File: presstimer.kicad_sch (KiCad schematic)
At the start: 28 parts, among them J1 Screw_Terminal_01x02, SW1 SW_Push, SW2 SW_Push, U1 AP7361C-33ER, U2 ESP32-S3-WROOM-1

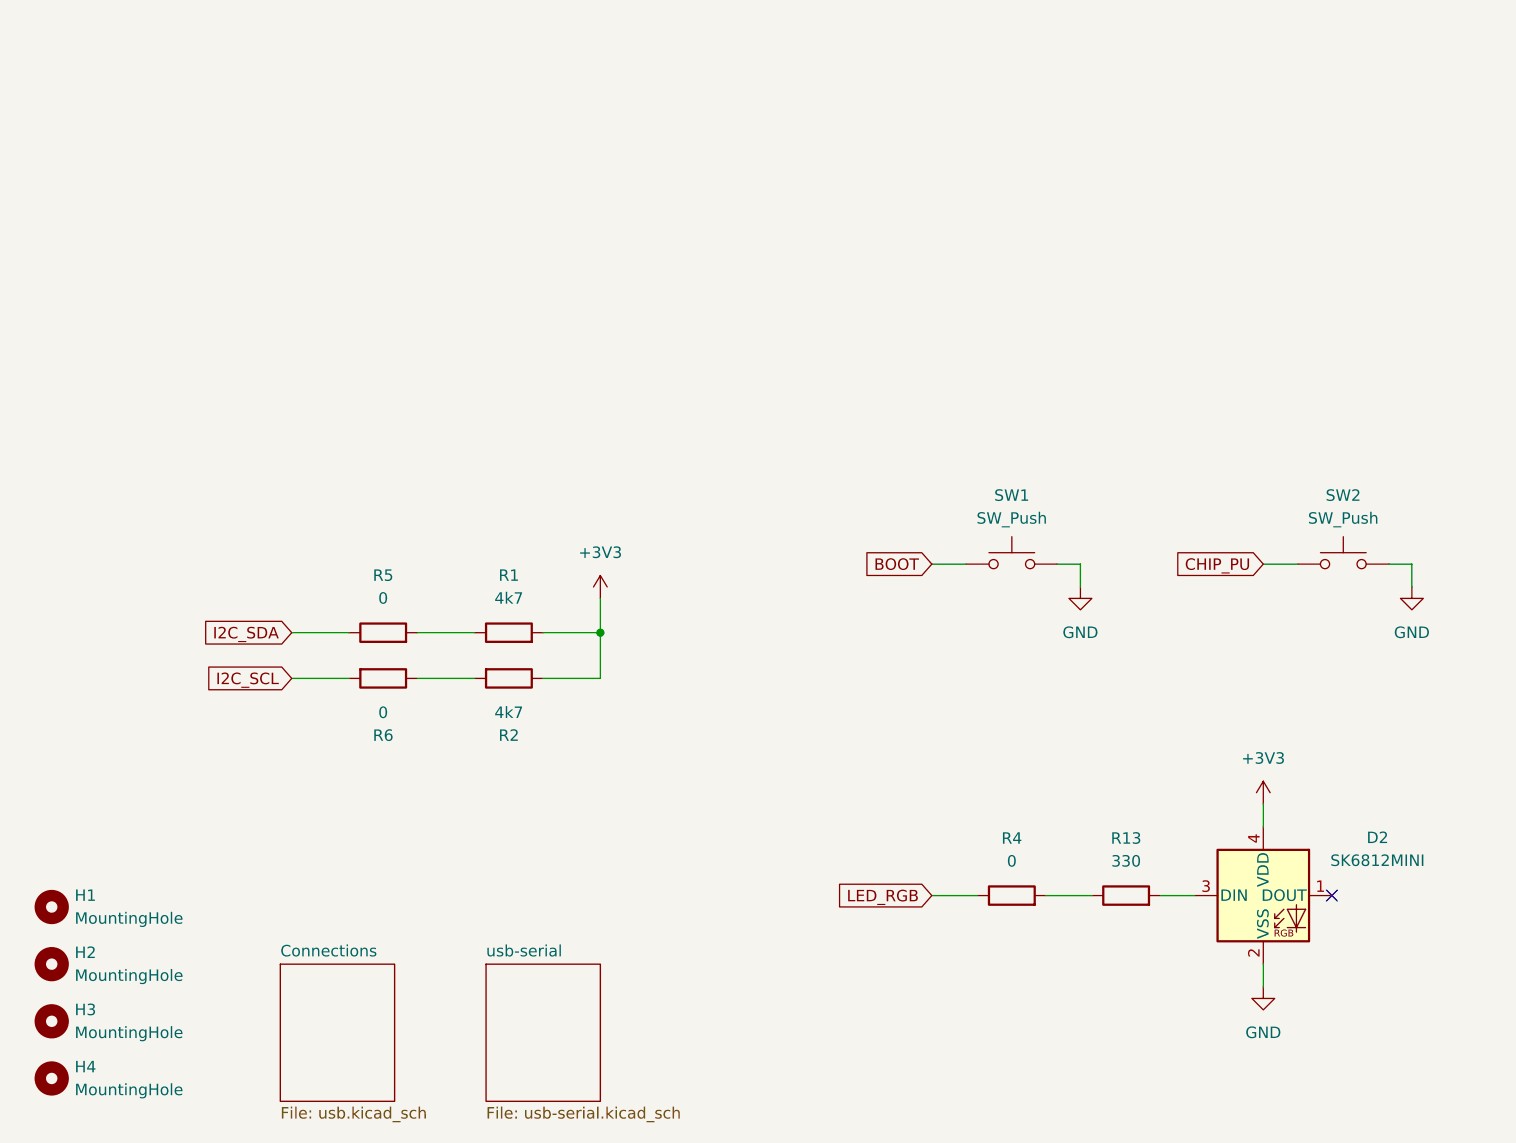
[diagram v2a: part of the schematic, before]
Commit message: before removal of cp2102
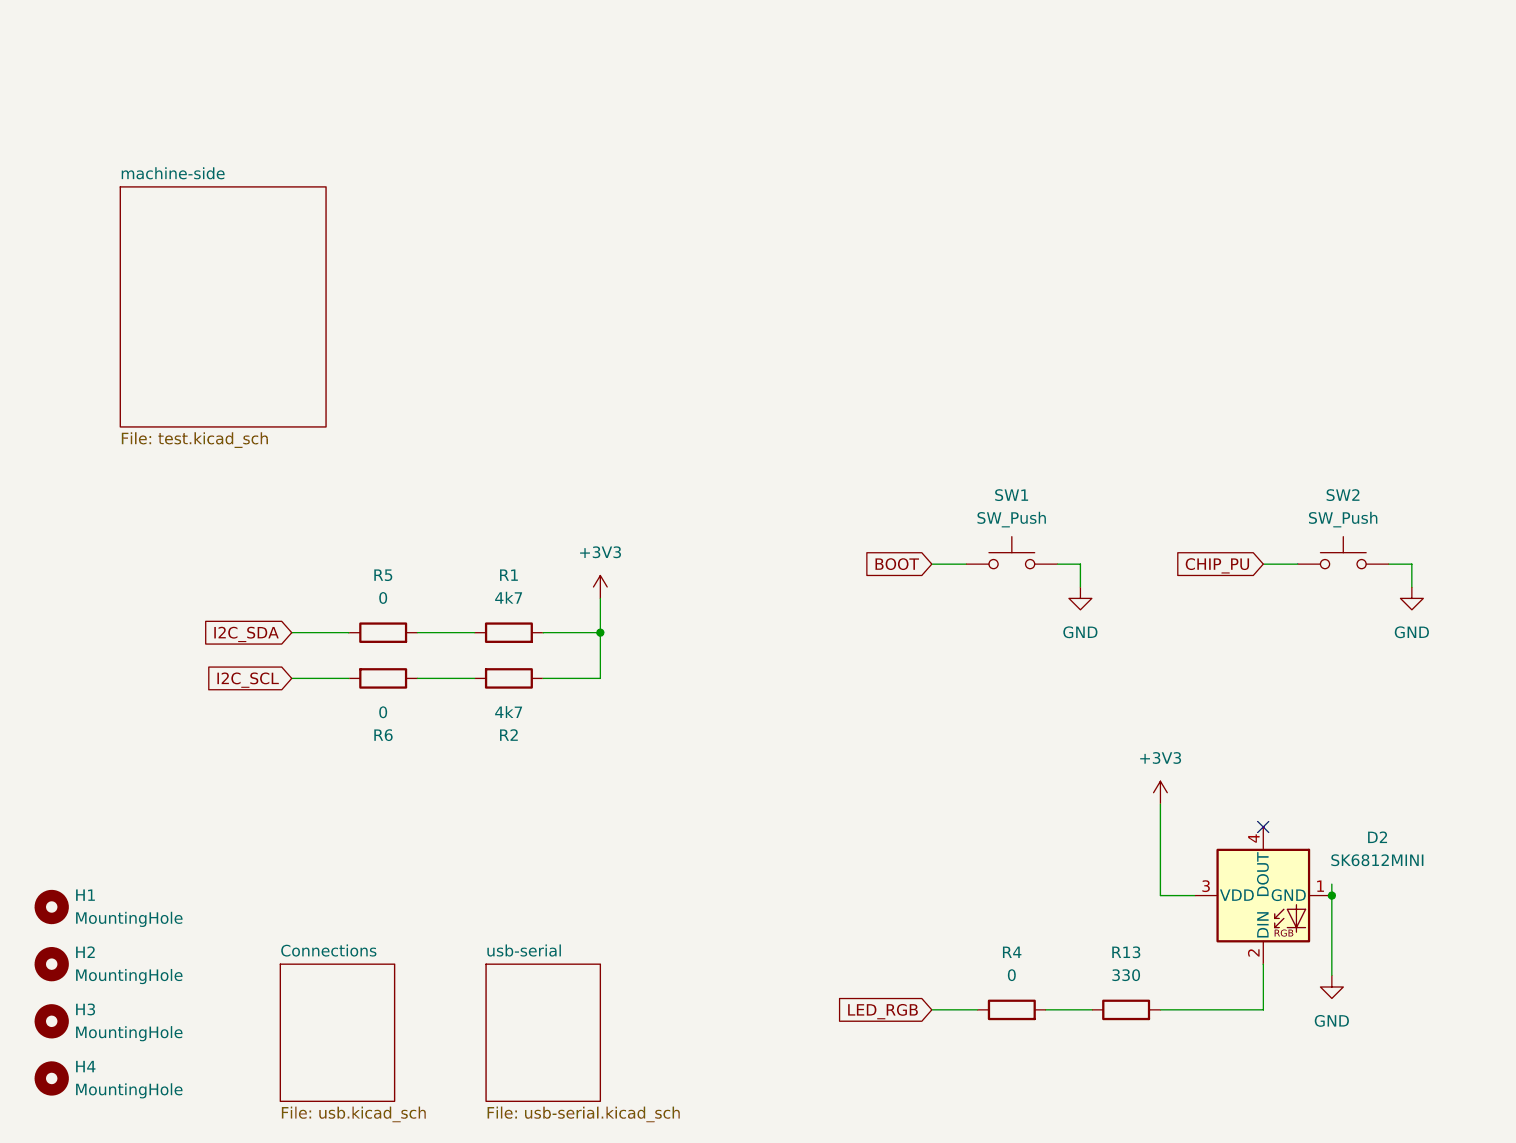
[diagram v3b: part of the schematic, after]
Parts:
- D2: footprint LED_SMD:LED_SK6812MINI_PLCC4_3.5x3.5mm_P1.75mm -> markus:SK6812MINI--HS-012_3.7x3.5mm; symbol LED:SK6812MINI -> markus:SK6812MINI
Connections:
- net +3V3: now also D2.3 (VDD); no longer D2.4 (VDD)
- net GND: now also D2.1 (GND); no longer D2.2 (VSS)
- net at R13.2: now also D2.2 (DIN); no longer D2.3 (DIN)
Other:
- added sheet machine-side (test.kicad_sch)
- moved on the sheet: R13, R4
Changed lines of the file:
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@@
 	)
 	(junction
+		(at 160.02 170.18)
+		(diameter 0)
+		(color 0 0 0 0)
+	)
+	(junction
 		(at 182.88 59.69)
 		(diameter 0)
@@
 	)
 	(no_connect
-		(at 160.02 170.18)
+		(at 152.4 162.56)
 	)
 	(no_connect
@@
 	(wire
 		(pts
+			(xy 160.02 170.18) (xy 160.02 179.07)
+		)
+		(stroke
+			(width 0)
+			(type default)
+		)
+	)
+	(wire
+		(pts
 			(xy 54.61 26.67) (xy 58.42 26.67)
 		)
@@
 	(wire
 		(pts
-			(xy 128.27 170.18) (xy 133.35 170.18)
+			(xy 128.27 182.88) (xy 133.35 182.88)
 		)
 		(stroke
@@
 	(wire
 		(pts
-			(xy 152.4 177.8) (xy 152.4 180.34)
+			(xy 160.02 168.91) (xy 160.02 170.18)
 		)
 		(stroke
@@
 	(wire
 		(pts
+			(xy 140.97 170.18) (xy 144.78 170.18)
+		)
+		(stroke
+			(width 0)
+			(type default)
+		)
+	)
+	(wire
+		(pts
 			(xy 182.88 60.96) (xy 182.88 59.69)
 		)
@@
 	(wire
 		(pts
-			(xy 115.57 170.18) (xy 120.65 170.18)
+			(xy 115.57 182.88) (xy 120.65 182.88)
 		)
 		(stroke
@@
 	(wire
 		(pts
-			(xy 140.97 170.18) (xy 144.78 170.18)
+			(xy 140.97 182.88) (xy 152.4 182.88)
 		)
 		(stroke
@@
 	(wire
 		(pts
-			(xy 152.4 160.02) (xy 152.4 162.56)
+			(xy 140.97 160.02) (xy 140.97 170.18)
 		)
 		(stroke
@@
 	(wire
 		(pts
+			(xy 152.4 177.8) (xy 152.4 182.88)
+		)
+		(stroke
+			(width 0)
+			(type default)
+		)
+	)
+	(wire
+		(pts
 			(xy 68.58 21.59) (xy 78.74 21.59)
 		)
@@
 	(global_label "LED_RGB"
 		(shape input)
-		(at 115.57 170.18 180)
+		(at 115.57 182.88 180)
 		(fields_autoplaced yes)
 		(effects
@@
 		)
 		(property "Intersheetrefs" "${INTERSHEET_REFS}"
-			(at 104.3601 170.18 0)
+			(at 104.3601 182.88 0)
 			(hide yes)
 			(show_name no)
@@
 	(symbol
 		(lib_id "power:+3V3")
-		(at 152.4 160.02 0)
+		(at 140.97 160.02 0)
 		(unit 1)
 		(body_style 1)
@@
 		(fields_autoplaced yes)
 		(property "Reference" "#PWR036"
-			(at 152.4 163.83 0)
+			(at 140.97 163.83 0)
 			(hide yes)
 			(show_name no)
@@
 		)
 		(property "Value" "+3V3"
-			(at 152.4 154.94 0)
+			(at 140.97 154.94 0)
 			(show_name no)
 			(do_not_autoplace no)
@@
 		)
 		(property "Footprint" ""
-			(at 152.4 160.02 0)
+			(at 140.97 160.02 0)
 			(hide yes)
 			(show_name no)
@@
 		)
 		(property "Datasheet" ""
-			(at 152.4 160.02 0)
+			(at 140.97 160.02 0)
 			(hide yes)
 			(show_name no)
@@
 		)
 		(property "Description" "Power symbol creates a global label with name \"+3V3\""
-			(at 152.4 160.02 0)
+			(at 140.97 160.02 0)
 			(hide yes)
 			(show_name no)
@@
 	(symbol
 		(lib_id "power:GND")
-		(at 152.4 180.34 0)
+		(at 160.02 179.07 0)
 		(unit 1)
 		(body_style 1)
@@
 		(fields_autoplaced yes)
 		(property "Reference" "#PWR037"
-			(at 152.4 186.69 0)
+			(at 160.02 185.42 0)
 			(hide yes)
 			(show_name no)
@@
 		)
 		(property "Value" "GND"
-			(at 152.4 185.42 0)
+			(at 160.02 184.15 0)
 			(show_name no)
 			(do_not_autoplace no)
@@
 		)
 		(property "Footprint" ""
-			(at 152.4 180.34 0)
+			(at 160.02 179.07 0)
 			(hide yes)
 			(show_name no)
@@
 		)
 		(property "Datasheet" ""
-			(at 152.4 180.34 0)
+			(at 160.02 179.07 0)
 			(hide yes)
 			(show_name no)
@@
 		)
 		(property "Description" "Power symbol creates a global label with name \"GND\" , ground"
-			(at 152.4 180.34 0)
+			(at 160.02 179.07 0)
 			(hide yes)
 			(show_name no)
@@
 	(symbol
 		(lib_id "Device:R")
-		(at 137.16 170.18 90)
+		(at 137.16 182.88 90)
 		(unit 1)
 		(body_style 1)
@@
 		(fields_autoplaced yes)
 		(property "Reference" "R13"
-			(at 137.16 163.83 90)
+			(at 137.16 176.53 90)
 			(show_name no)
 			(do_not_autoplace no)
@@
 		)
 		(property "Value" "330"
-			(at 137.16 166.37 90)
+			(at 137.16 179.07 90)
 			(show_name no)
 			(do_not_autoplace no)
@@
 		)
 		(property "Footprint" "PCM_JLCPCB:R_0603"
-			(at 137.16 171.958 90)
+			(at 137.16 184.658 90)
 			(hide yes)
 			(show_name no)
@@
 		)
 		(property "Datasheet" ""
-			(at 137.16 170.18 0)
+			(at 137.16 182.88 0)
 			(hide yes)
 			(show_name no)
@@
 		)
 		(property "Description" "Resistor"
-			(at 137.16 170.18 0)
+			(at 137.16 182.88 0)
 			(hide yes)
 			(show_name no)
@@
 		)
 		(property "LCSC" "C105881"
-			(at 137.16 163.83 0)
+			(at 137.16 176.53 0)
 			(hide yes)
 			(show_name no)
@@
 	(symbol
 		(lib_id "Device:R")
-		(at 124.46 170.18 90)
+		(at 124.46 182.88 90)
 		(unit 1)
 		(body_style 1)
@@
 		(fields_autoplaced yes)
 		(property "Reference" "R4"
-			(at 124.46 163.83 90)
+			(at 124.46 176.53 90)
 			(show_name no)
 			(do_not_autoplace no)
@@
 		)
 		(property "Value" "0"
-			(at 124.46 166.37 90)
+			(at 124.46 179.07 90)
 			(show_name no)
 			(do_not_autoplace no)
@@
 		)
 		(property "Footprint" "PCM_JLCPCB:R_0805"
-			(at 124.46 171.958 90)
+			(at 124.46 184.658 90)
 			(hide yes)
 			(show_name no)
@@
 		)
 		(property "Datasheet" ""
-			(at 124.46 170.18 0)
+			(at 124.46 182.88 0)
 			(hide yes)
 			(show_name no)
@@
 		)
 		(property "Description" "Resistor"
-			(at 124.46 170.18 0)
+			(at 124.46 182.88 0)
 			(hide yes)
 			(show_name no)
@@
 		)
 		(property "LCSC" "C17477"
-			(at 124.46 163.83 0)
+			(at 124.46 176.53 0)
 			(hide yes)
 			(show_name no)
@@
 	)
 	(symbol
-		(lib_id "LED:SK6812MINI")
+		(lib_id "markus:SK6812MINI")
 		(at 152.4 170.18 0)
 		(unit 1)
@@
 			)
 		)
-		(property "Footprint" "LED_SMD:LED_SK6812MINI_PLCC4_3.5x3.5mm_P1.75mm"
+		(property "Footprint" "markus:SK6812MINI--HS-012_3.7x3.5mm"
 			(at 153.67 177.8 0)
 			(hide yes)
@@
 			)
 		)
-		(property "Datasheet" "https://cdn-shop.adafruit.com/product-files/2686/SK6812MINI_REV.01-1-2.pdf"
+		(property "Datasheet" "https://www.lcsc.com/datasheet/C2922787.pdf?spm=wm.sxq.inf.ggs&lcsc_vid=QVVYX1NTFAIPVVxTQgALBVECRllfVVIARQcPUVUFR1MxVlNeTlVXV1RfRFZcXzsOAxUeFF5JWBYZEEoBGA4JCwFIFA4DSA%3D%3D"
 			(at 154.94 179.705 0)
 			(hide yes)
@@
 				)
 			)
+		)
+	)
+	(sheet
+		(at 25.4 91.44)
+		(size 22.86 26.67)
+		(exclude_from_sim no)
+		(in_bom yes)
+		(on_board yes)
+		(dnp no)
+		(fields_autoplaced yes)
+		(stroke
+			(width 0.1524)
+			(type solid)
+		)
+		(fill
+			(color 0 0 0 0)
+		)
+		(property "Sheetname" "machine-side"
+			(at 25.4 90.7284 0)
+			(show_name no)
+			(do_not_autoplace no)
+			(effects
+				(font
+					(size 1.27 1.27)
+				)
+				(justify left bottom)
+			)
+		)
+		(property "Sheetfile" "test.kicad_sch"
+			(at 25.4 118.6946 0)
+			(show_name no)
+			(do_not_autoplace no)
+			(effects
+				(font
+					(size 1.27 1.27)
+				)
+				(justify left top)
+			)
+		)
+		(instances
+			(project "presstimer"
+				(path "/63494a82-20b5-470b-977d-6a82bfa70174"
+					(page "4")
+				)
+			)
